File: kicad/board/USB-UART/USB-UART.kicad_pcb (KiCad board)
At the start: 2 copper layers, 34.5 x 17 mm, 17 parts, among them J1 Conn_01x05, J2 Conn_01x02, J3 USB_B_Micro, Q1 MMBF170, U1 MCP2221AxSL

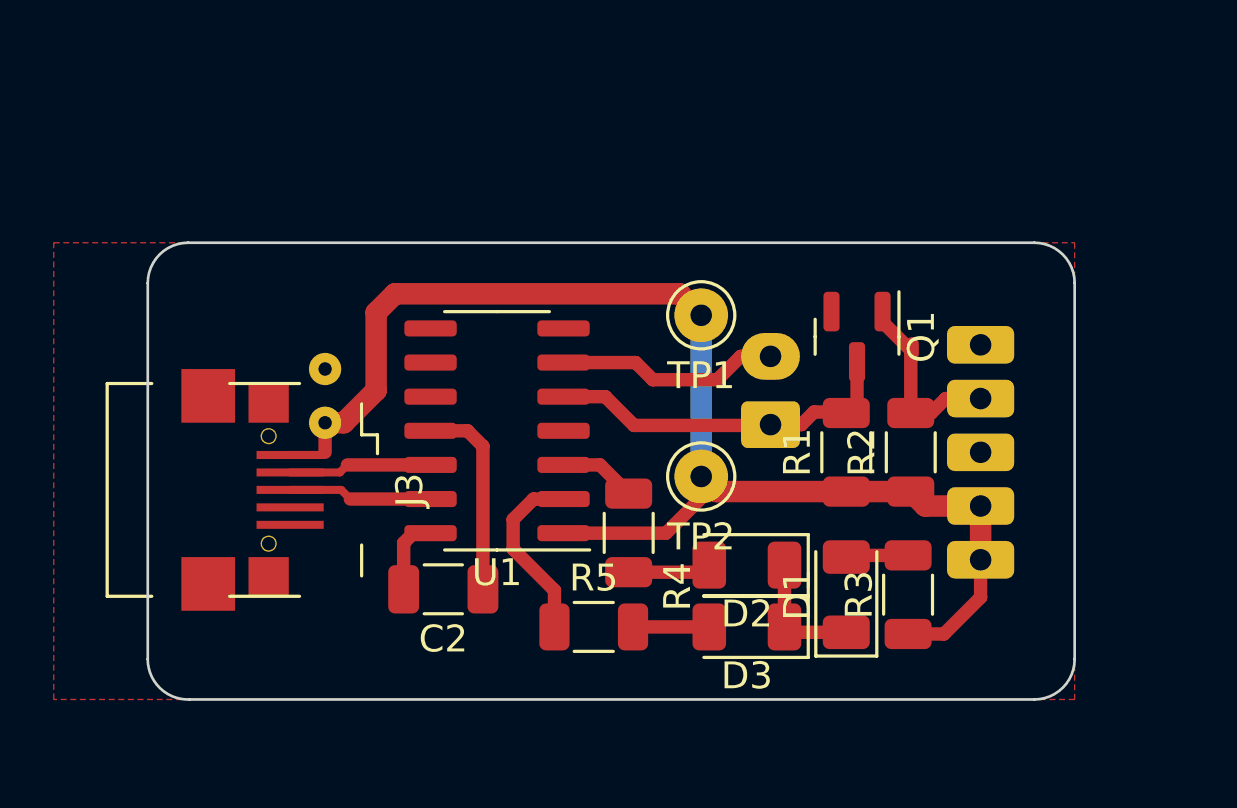
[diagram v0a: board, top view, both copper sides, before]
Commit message: hardware: korrekturen fehlerhaftes pcb
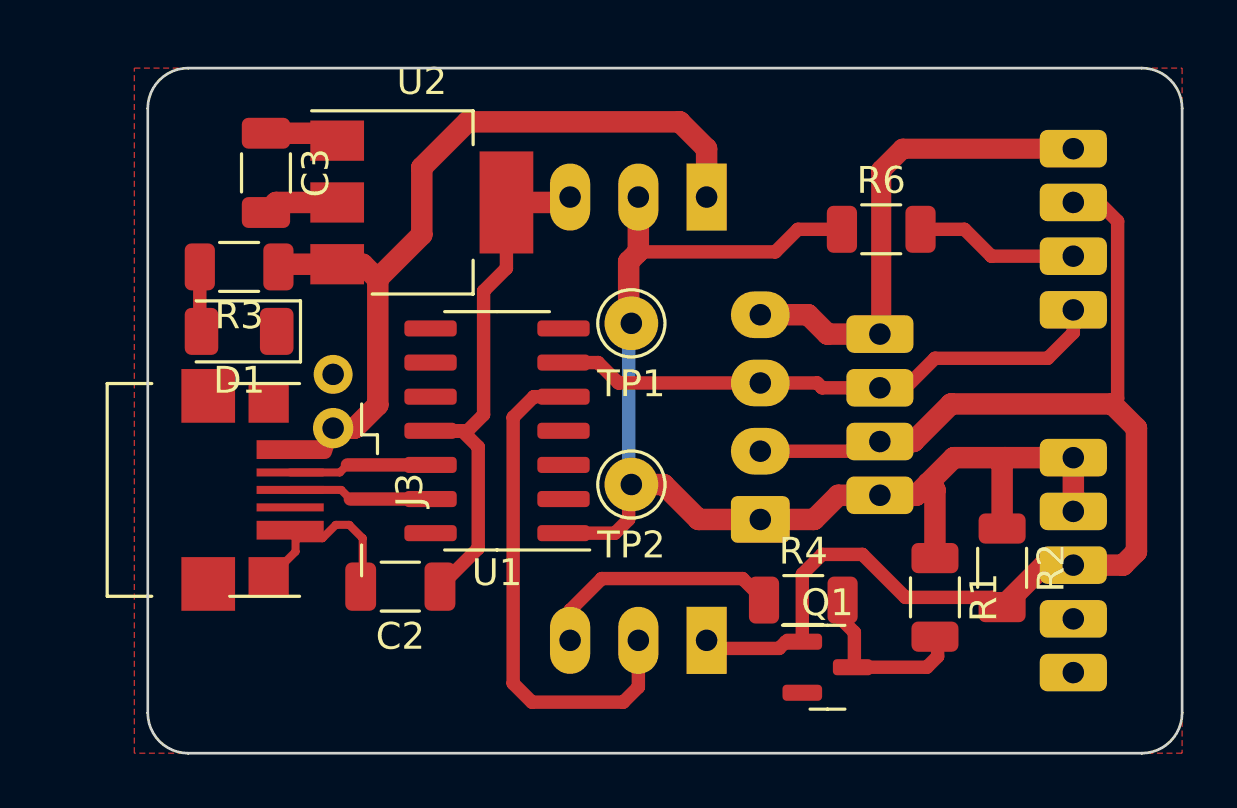
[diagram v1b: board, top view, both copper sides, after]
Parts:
- removed D2, D3: LED, LED_SMD:LED_1206_3216Metric
- removed J2: Conn_01x02, Connector_Molex:Molex_KK-254_AE-6410-02A_1x02_P2.54mm_Vertical
- removed R5: 1K, Resistor_SMD:R_1206_3216Metric
- added C3: 1u, Capacitor_SMD:C_1206_3216Metric, F.Cu at (109.9, 98.4)
- added J1: Conn_01x04, Connector_Molex:Molex_KK-254_AE-6410-04A_1x04_P2.54mm_Vertical, B.Cu at (128.3, 111.3)
- added R6: 100, Resistor_SMD:R_1206_3216Metric, F.Cu at (132.8, 100.5)
- added SW1: SW_SPDT, Button_Switch_THT:SW_Slide_1P2T_CK_OS102011MS2Q, B.Cu at (126.3, 99.3)
- added SW2: SW_SPDT, Button_Switch_THT:SW_Slide_1P2T_CK_OS102011MS2Q, B.Cu at (126.3, 115.8)
- added Sol0: Conn_01x04, Connector_JST:JST_PH_B4B-PH-K_1x04_P2.00mm_Vertical, B.Cu at (139.9, 97.5)
- added Sol1: Conn_01x04, Connector_JST:JST_PH_B4B-PH-K_1x04_P2.00mm_Vertical, B.Cu at (132.8, 104.4)
- added U2: LM1117-3.3, Package_TO_SOT_SMD:SOT-223-3_TabPin2, F.Cu at (115.7, 99.5)
- R4: value 1K -> 10
- moved R3 27.7 mm to (108.9, 101.9), turned to 180 degrees
- moved D1 24.6 mm to (108.9, 104.3), turned to 180 degrees
- moved Q1 12.3 mm to (130.8, 116.8), turned to 0 degrees
- moved R4 6.96 mm to (129.9, 114.3), turned to 0 degrees
- moved R1 6.33 mm to (134.8, 114.2), turned to -90 degrees
- moved R2 5.48 mm to (137.3, 113.1), turned to -90 degrees
- moved SmartM0 5.13 mm to (139.9, 109.0), turned to -90 degrees
- moved TP1 2.62 mm to (123.5, 104.0)
- moved TP2 2.62 mm to (123.5, 110.0)
- moved C1 1.82 mm to (112.4, 105.9), turned to -90 degrees
- moved C2 1.60 mm to (114.9, 113.8)
- renumbered J1 to SmartM0
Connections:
- net Net-(C2-Pad1) renamed +3V3
- C1 pad 1: +5V -> GND
- C1 pad 2: GND -> +5V
- Q1 pad 1: Net-(J1-Pad4) -> Rx_
- Q1 pad 3: Net-(U1-Pad5) -> Net-(Q1-Pad3)
- R1 pad 1: +5V -> SupplyVoltage
- R1 pad 2: Net-(U1-Pad5) -> Net-(Q1-Pad3)
- R2 pad 1: +5V -> SupplyVoltage
- R2 pad 2: Net-(J1-Pad4) -> Rx_
- R4 pad 1: Net-(U1-Pad3) -> Rx_inv
- R4 pad 2: Net-(D2-Pad2) -> Net-(Q1-Pad3)
- SmartM0 pad 1: +5V -> SupplyVoltage
- SmartM0 pad 2: +5V -> SupplyVoltage
- SmartM0 pad 3: GND -> Rx_
- SmartM0 pad 4: Net-(J1-Pad4) -> GND
- TP1 pad 1: +5V -> SupplyVoltage
- TP2 pad 1: +5V -> SupplyVoltage
- U1 pad 1: +5V -> SupplyVoltage
- U1 pad 2: Net-(U1-Pad2) -> unconnected-(U1-Pad2)
- U1 pad 3: Net-(U1-Pad3) -> unconnected-(U1-Pad3)
- U1 pad 5: Net-(U1-Pad5) -> Rx
- U1 pad 6: Net-(J2-Pad2) -> Tx
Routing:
- net Rx_: track 0.00 -> 49.8 mm
- net SupplyVoltage: track 0.00 -> 48.3 mm
- net Tx: track 0.00 -> 21.1 mm
- net GND: track 7.56 -> 27.8 mm
- net +5V: track 50.4 -> 31.3 mm
- net Rx: track 0.00 -> 19.0 mm
- net +3V3: track 8.06 -> 23.5 mm
- net Net-(U1-Pad5): track 13.6 -> 0.00 mm
- net Rx_inv: track 0.00 -> 9.16 mm
- net Net-(J2-Pad2): track 8.33 -> 0.00 mm
- net Net-(J1-Pad4): track 7.03 -> 0.00 mm
- net Net-(U1-Pad2): track 6.83 -> 0.00 mm
- net Net-(Q1-Pad3): track 0.00 -> 6.81 mm
- net Net-(Sol0-Pad3): track 0.00 -> 6.10 mm
- net Net-(D2-Pad2): track 3.11 -> 0.00 mm
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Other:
- board size 34.5 x 17 mm -> 38.5 x 25.5 mm
- board text added: "3V3"
- board text added: "5V"
- board text added: "Gnd Tx Rx V+"
- board text added: "RX"
- board text added: "Smartmeter"
- board text added: "Soladin"
- board text added: "invert RX"
